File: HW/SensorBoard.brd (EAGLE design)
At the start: 50 x 50 mm, 24 parts, among them U1 ATMEGA328P_TQFP, X1 16mhz

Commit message: V1.0
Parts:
- removed C6: 100uf, rcl:153CLV-0505
- added C5: 100uf, rcl:C1206
- added SW: (no value), adafruit:BTN_CK_KSS
- SW1: device adafruit:BTN_CK_KSS -> SparkFun-Switches:TACTILE_SWITCH_SMD_5.2MM
- UART: device pinhead:1X02 -> pinhead:1X04
- X1: value 16mhz -> 7B-16.000MAAJ-T; device Crystals:FC4SDCBMF16.0-T1 -> Crystals:7B-16.000MAAJ-T
- X2: value (none) -> FC4SDCBMF16.0-T1; device Crystals:XTAL_HC49 -> Crystals:FC4SDCBMF16.0-T1
- moved SW1 2.03 mm to (-20.6, 11.4), turned to 0 degrees
- moved X2 1.00 mm to (8.00, 0.00), flipped to the bottom
- turned X1 to 90 degrees
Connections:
- new net ADDR_SENSE: U1.24, UART.3
- net +5V: now also C5.1; no longer C6.+
- net GND: now also C5.2, SW.P$2, SW1.3, SW1.4, UART.4; no longer C6.-, SW1.P$2
- net N$1: now also X1.3; no longer X1.1
- net N$2: now also X1.1; no longer X1.2
- net RESET: now also SW.P$1, SW1.1, SW1.2; no longer SW1.P$1
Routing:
- net ADDR_SENSE: track 0.00 -> 23.7 mm, vias 0 -> 1
- net GND: track 39.4 -> 46.9 mm, vias 7 -> 6
- net N$1: track 13.3 -> 16.8 mm, vias 0 -> 1
- net RESET: track 44.0 -> 45.8 mm
- net N$2: track 15.6 -> 17.0 mm
- net TXD: track 14.0 -> 15.1 mm
- net RXD: track 13.8 -> 14.8 mm
- net SDA: track 67.6 -> 66.8 mm
- net +5V: track 43.2 -> 43.7 mm
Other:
- board text added: "0X___"
- board text added: "Addr"
- board text added: "RXD"
- board text added: "TXD"
- board text removed: "0X_ _"

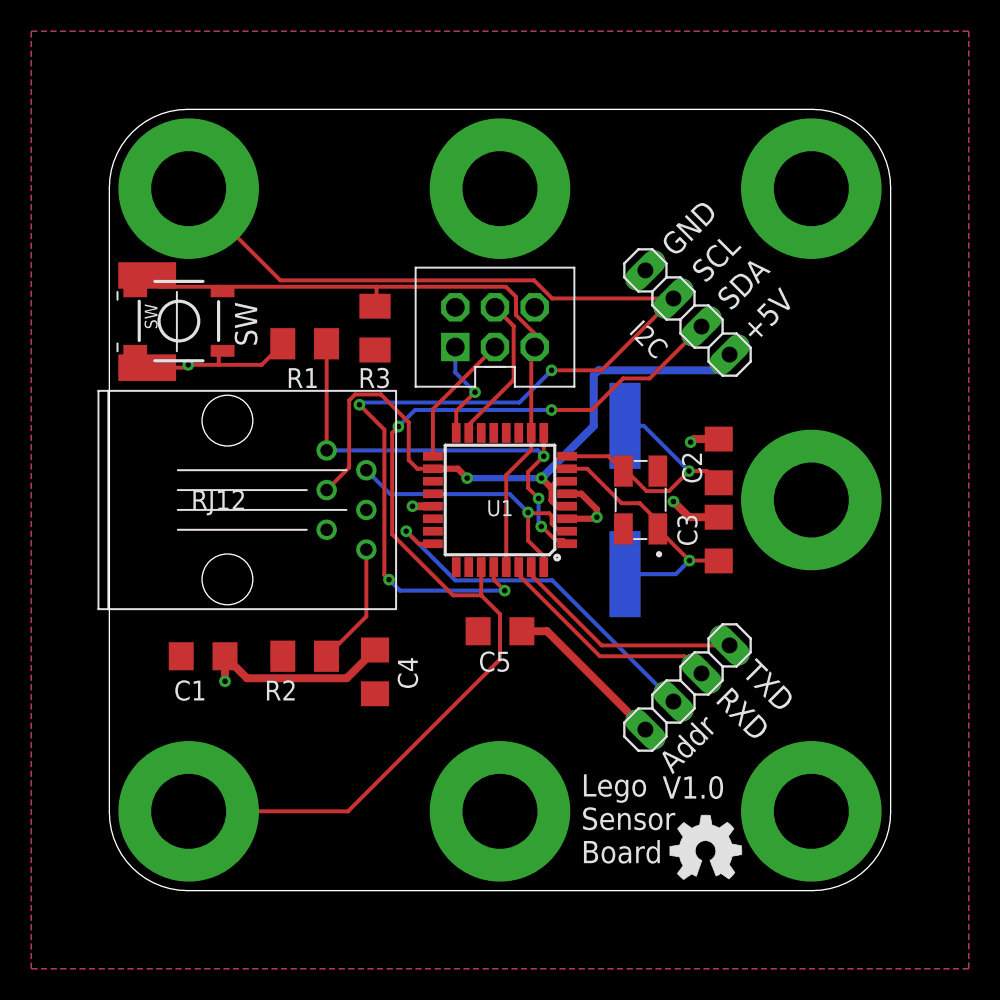
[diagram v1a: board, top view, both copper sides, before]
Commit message: adding signalisation leds
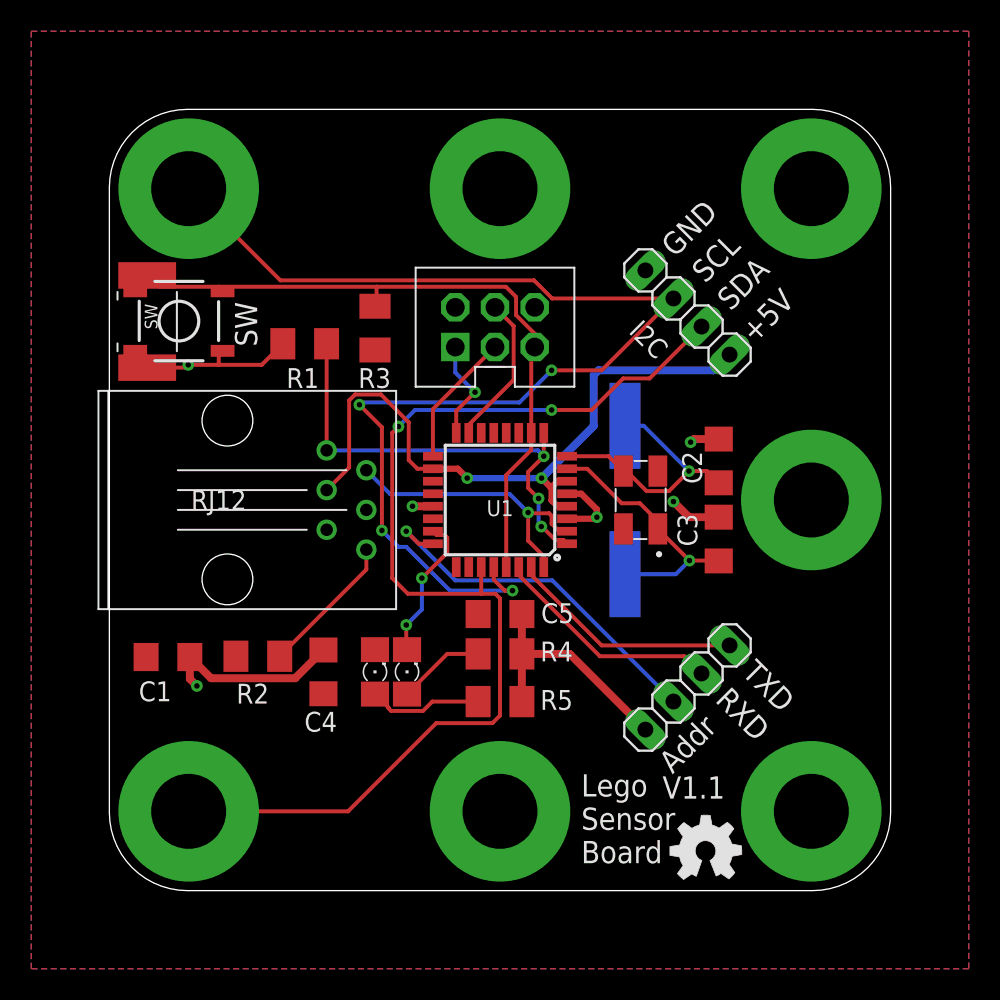
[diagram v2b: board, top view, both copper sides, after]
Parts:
- added LED1: POWER, led:1206
- added LED2: STATUS, led:1206
- added R4, R5: 1K, rcl:M1206
- moved C4 3.30 mm to (-11.3, -11.0)
- moved R2 3.00 mm to (-15.5, -10.0)
- moved C1 2.25 mm to (-21.2, -10.1)
- moved C5 1.10 mm to (0.00, -7.30)
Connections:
- new net N$3: LED2.A, R4.1
- new net N$4: LED1.A, R5.1
- new net STATUS: LED2.C, U1.23
- net +5V: now also LED1.C
- net GND: now also R4.2, R5.2
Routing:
- net STATUS: track 0.00 -> 9.36 mm, vias 0 -> 2
- net N$4: track 0.00 -> 7.32 mm
- net N$3: track 0.00 -> 5.62 mm
- net GND: track 46.9 -> 51.2 mm
- net SDA: track 66.8 -> 71.0 mm
- net S_A: track 7.88 -> 9.12 mm
- net SCL: track 78.3 -> 77.7 mm
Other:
- board text added: "V1.1"
- board text removed: "V1.0"
